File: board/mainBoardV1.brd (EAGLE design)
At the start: 41.9 x 14.9 mm, 11 parts, among them U1 STM32F051C8T

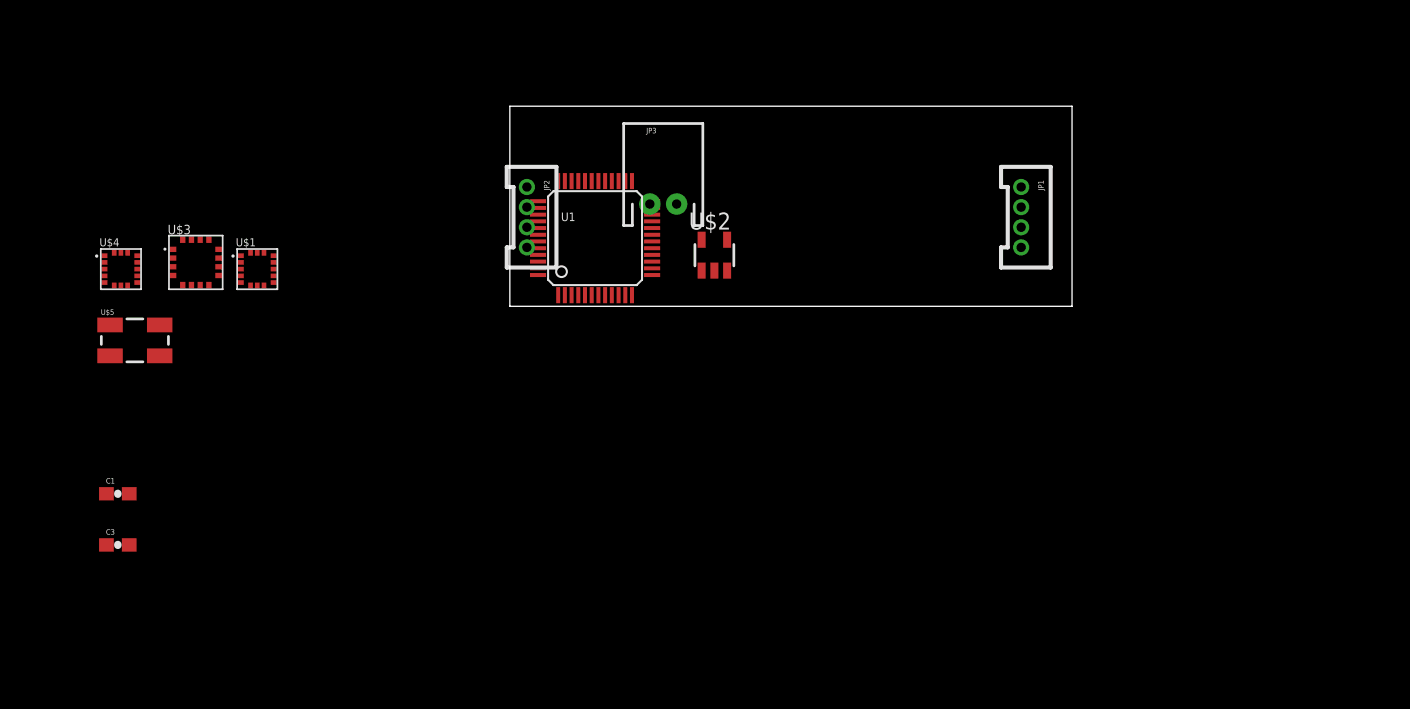
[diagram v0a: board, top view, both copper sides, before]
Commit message: initial board + LPC MCU
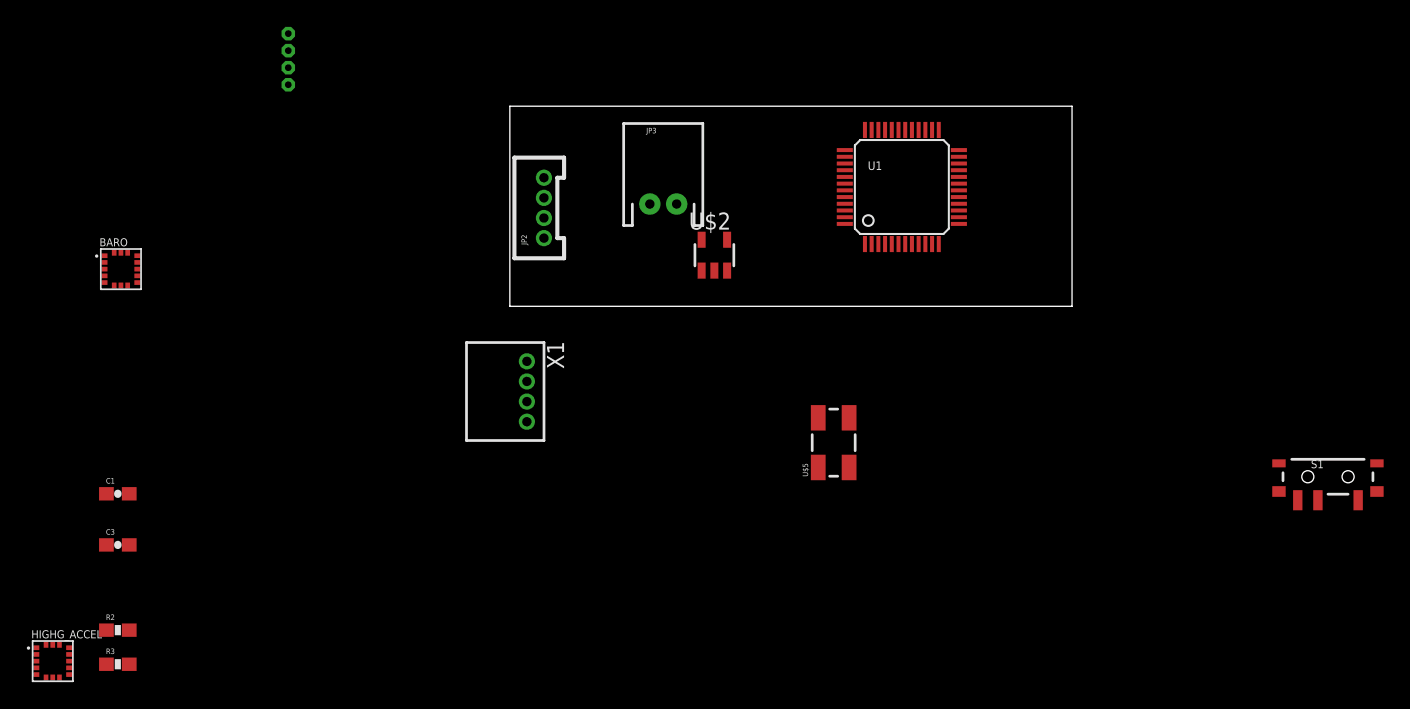
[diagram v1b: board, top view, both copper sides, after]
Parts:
- removed U$1: LIS3DSH, Sensors:LGA-16-3X3X1
- removed U$3: L3G4200D, Sensors:LGA-16L-4X4X1.1
- added HIGHG_ACCEL: LPS331AP, Sensors:LGA-16-3X3X1
- added R2, R3: pullup, SparkFun-Passives:0603-RES
- added S1: (no value), SparkFun-Electromechanical:SWITCH-SPST-SMD-A
- added X1: S4B-ZR, con-jst:S4B-ZR
- JP1: value (none) -> M4; device SparkFun-Connectors:1X04-1.5MM_JST -> Connector:M.5_4
- moved JP1 55.8 mm to (-16.5, 20.3)
- moved U$5 52.6 mm to (24.1, -10.2), turned to 90 degrees
- moved U1 23.2 mm to (29.2, 8.89)
- moved JP2 4.02 mm to (2.54, 5.08), turned to 90 degrees
- renumbered U$4 to BARO
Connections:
- removed net VDD: U1.1, U1.24, U1.48
- removed net VDDA: U1.9
- new net I2C1_SCL: BARO.4, HIGHG_ACCEL.4, R3.2, U1.21
- new net I2C1_SDA: BARO.6, HIGHG_ACCEL.6, R2.2, U1.22
- new net I2C2_SCL: U1.35
- new net I2C2_SDA: U1.36
- new net USART1_RX: U1.31
- new net USART1_TX: U1.30
- net 3.3V: now also BARO.1, BARO.15, HIGHG_ACCEL.1, HIGHG_ACCEL.14, HIGHG_ACCEL.15, R2.1, R3.1, U1.1, U1.24, U1.48, U1.9; no longer U$1.14, U$1.15, U$3.15, U$3.16
- net GND: now also HIGHG_ACCEL.10, HIGHG_ACCEL.12, HIGHG_ACCEL.13, HIGHG_ACCEL.16, HIGHG_ACCEL.5, U1.44, U1.7; no longer U$1.10, U$1.12, U$1.13, U$1.16, U$1.2, U$1.3, U$1.5

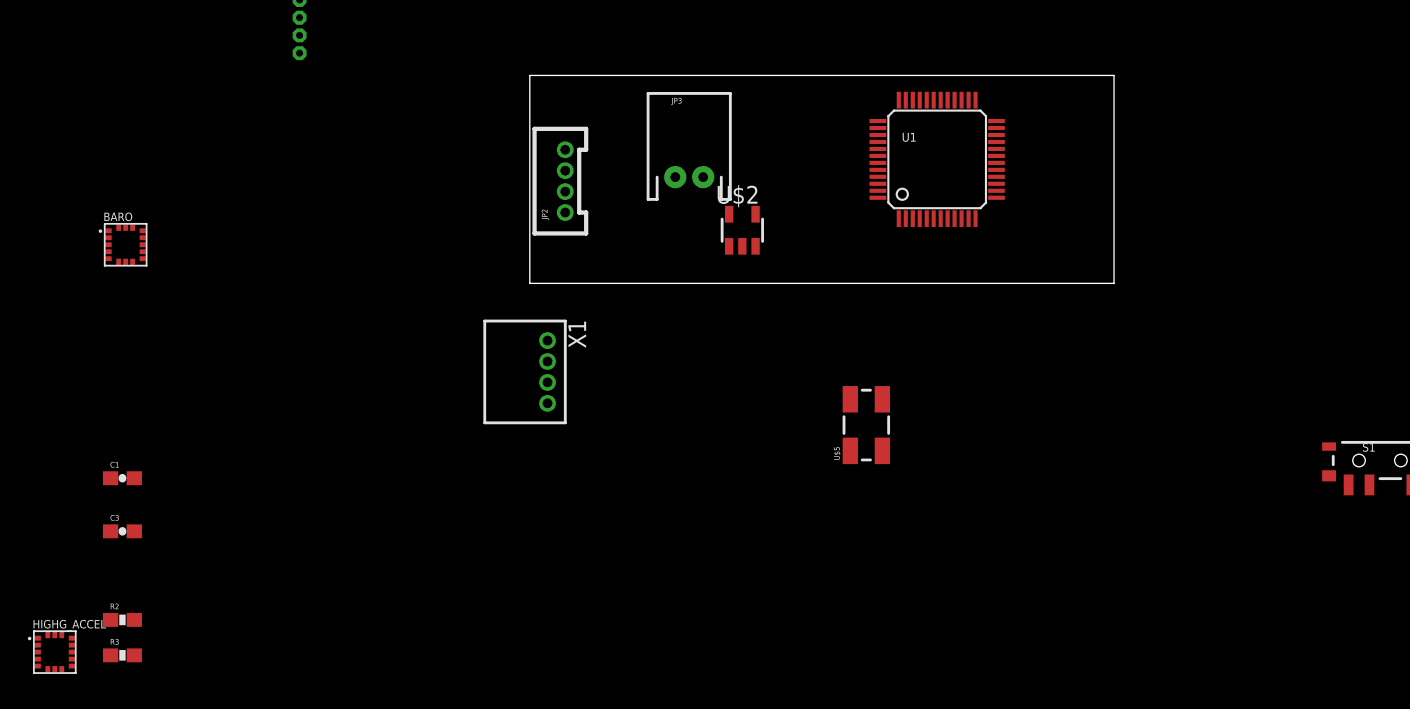
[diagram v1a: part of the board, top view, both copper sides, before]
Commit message: all major components on board, we have very little space
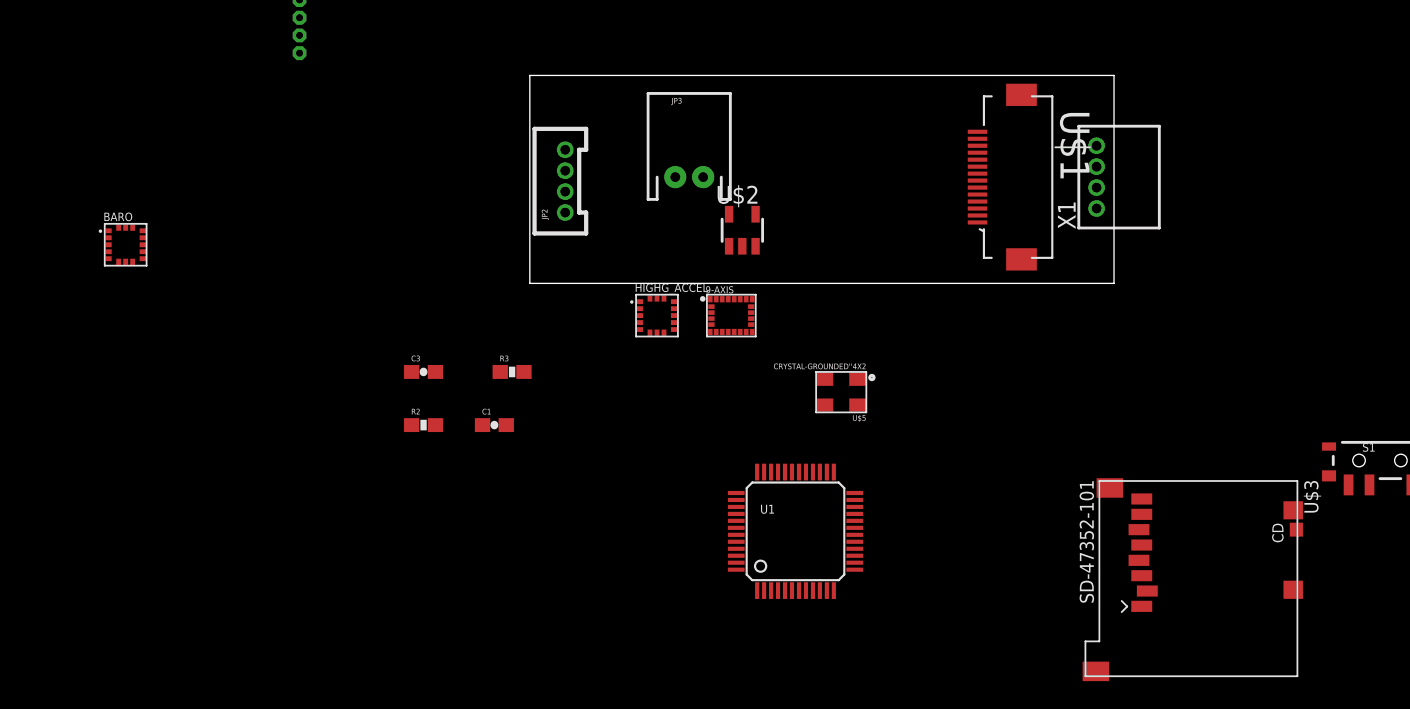
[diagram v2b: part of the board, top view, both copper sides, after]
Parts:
- added 9-AXIS: LSM9DS1, Sensors:LGA-24L-3.5X3X1
- added U$1: ER-OLED0.84-1, Sensors:MOLEX_52892-1433
- added U$3: MICROSD-CD, Sensors:MOLEX_SD-47352-101
- U$5: value CRYSTAL-GROUNDED -> CRYSTAL-GROUNDED''4X2; device SparkFun-FreqCtrl:CRYSTAL-SMD-5X3 -> SparkFun-FreqCtrl:CRYSTAL-SMD-4X2
- U1: value STM32F051C8T -> (none); device STM32F030:LQFP48 -> LPC11U68:LQFP48
- moved HIGHG_ACCEL 49.5 mm to (7.62, -3.81)
- moved X1 41.8 mm to (40.6, 7.62), turned to 90 degrees
- moved R3 34.5 mm to (-1.27, -6.35)
- moved U1 28.5 mm to (19.1, -17.8)
- moved C1 26.9 mm to (-2.54, -10.2)
- moved R2 25.7 mm to (-7.62, -10.2)
- moved C3 24.4 mm to (-7.62, -6.35)
- moved U$5 3.81 mm to (24.1, -6.35), turned to 180 degrees
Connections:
- removed net I2C1_SCL: BARO.4, HIGHG_ACCEL.4, R3.2, U1.21
- removed net I2C1_SDA: BARO.6, HIGHG_ACCEL.6, R2.2, U1.22
- removed net I2C2_SCL: U1.35
- removed net I2C2_SDA: U1.36
- removed net USART1_RX: U1.31
- removed net USART1_TX: U1.30
- new net I2C0_SCL: 9-AXIS.2, BARO.4, HIGHG_ACCEL.4, R3.2, U1.15
- new net I2C0_SDA: 9-AXIS.4, BARO.6, HIGHG_ACCEL.6, R2.2, U1.16
- net 3.3V: no longer U1.1, U1.24, U1.48, U1.9
- net GND: now also U$5.P$1, U$5.P$4; no longer U$5.2, U$5.4, U1.23, U1.44, U1.47, U1.7, U1.8
- net N$2: now also U$5.P$2, U1.7; no longer U$5.3, U1.5
- net N$3: now also U$5.P$3; no longer U$5.1

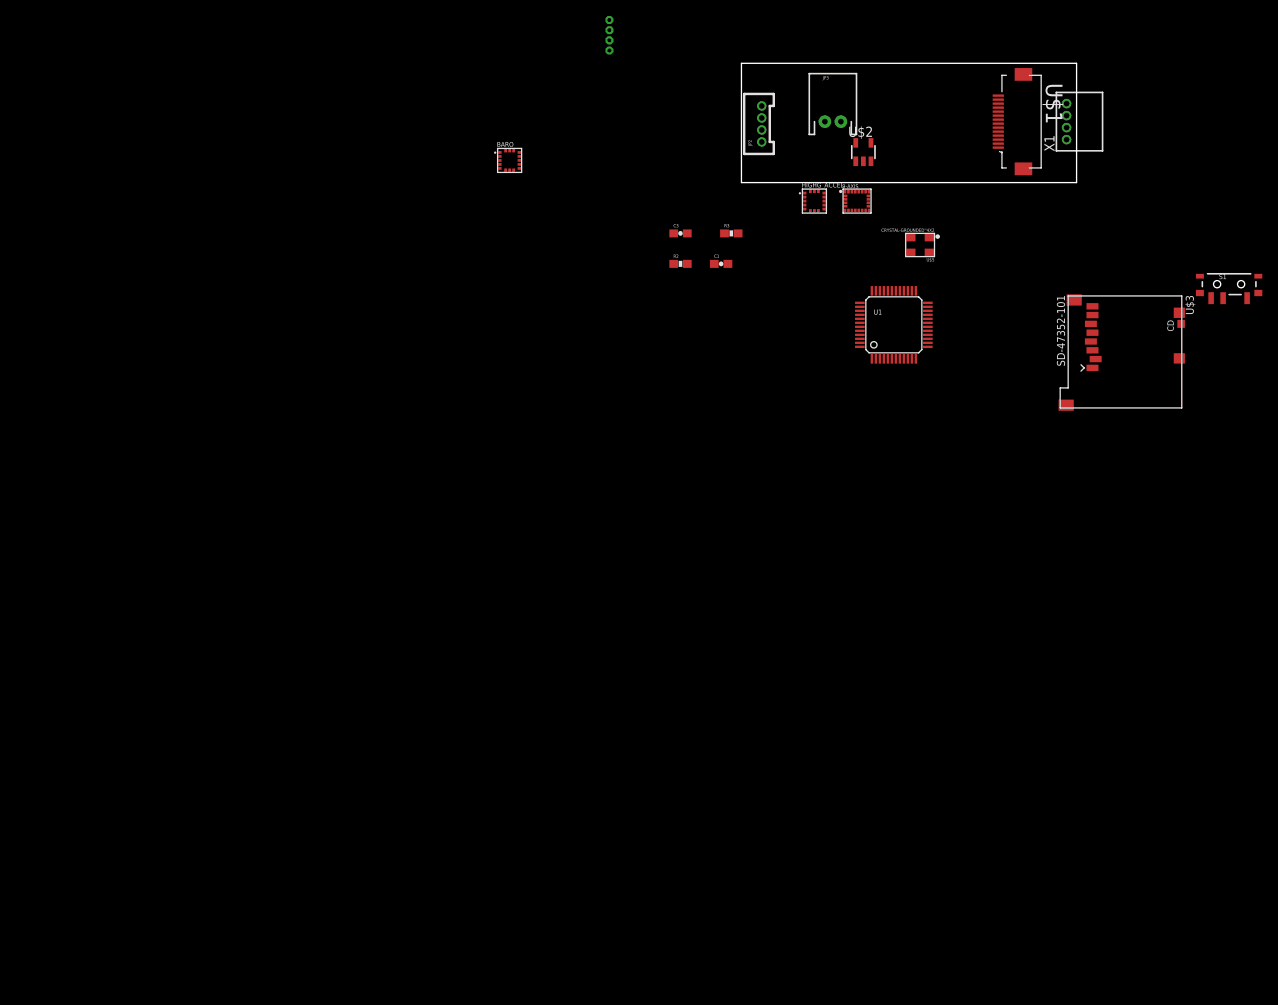
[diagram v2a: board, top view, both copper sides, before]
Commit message: board schematic ready for design review
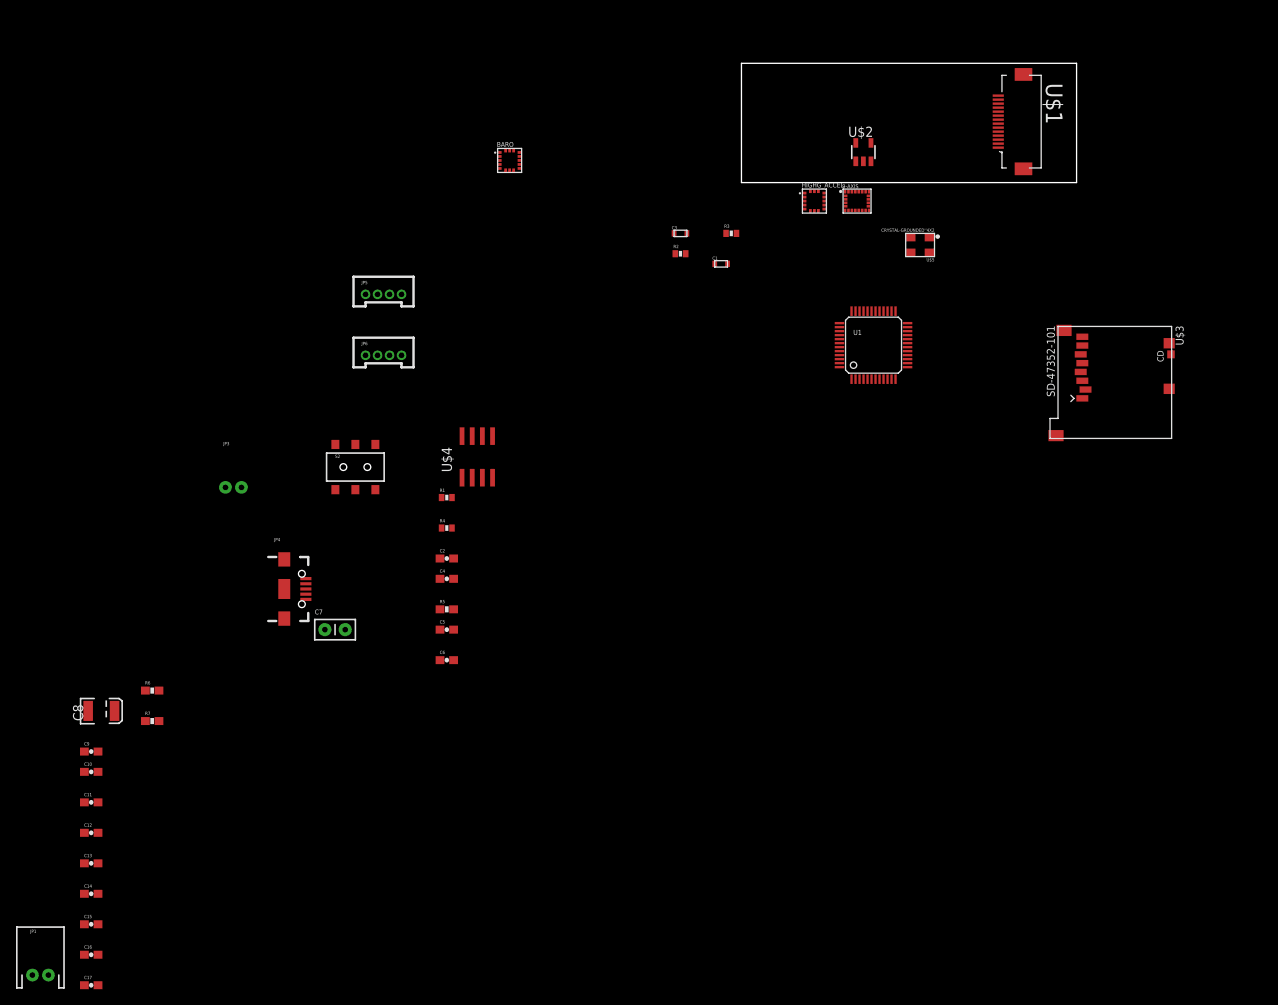
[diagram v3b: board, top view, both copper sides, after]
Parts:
- removed JP2: (no value), SparkFun-Connectors:1X04-1.5MM_JST
- removed S1: (no value), SparkFun-Electromechanical:SWITCH-SPST-SMD-A
- removed X1: S4B-ZR, con-jst:S4B-ZR
- added C10, C14, C15: 1uF, SparkFun-Passives:0603-CAP
- added C11, C16, C17: 0.1uF, SparkFun-Passives:0603-CAP
- added C12, C13, C9: 10uF, SparkFun-Passives:0603-CAP
- added C2, C4: 1uF, SparkFun-Capacitors:0603-CAP
- added C5, C6: 2.2uF, SparkFun-Capacitors:0603-CAP
- added C7: 10nF, SparkFun-Capacitors:CAP-PTH-SMALL2
- added C8: 10uF, SparkFun-Capacitors:EIA3528
- added JP4: USB_MICROB_PLUGCONN-11752, SparkFun-Connectors:USB-B-MICRO-SMD_V03
- added JP5, JP6: (no value), SparkFun-Connectors:1X04-1.5MM_JST
- added R1, R4: pullup, SparkFun-Passives:0402-RES
- added R5: (no value), SparkFun-Resistors:0603-RES
- added R6, R7: 33, SparkFun-Passives:0603-RES
- added S2: DPDT, SparkFun-Electromechanical:AYZ0202
- added U$4: P82B715, Sensors:SO8
- C1, C3: device SparkFun-Passives:0603-CAP -> ELL-i-Passives:C0603
- JP1: value M4 -> M02JST-PTH-2; device Connector:M.5_4 -> SparkFun-Connectors:JST-2-PTH
- JP3: value M02JST-PTH-2 -> M02-JST-2-PTH-NO_SILK; device SparkFun-Connectors:JST-2-PTH -> SparkFun-Connectors:JST-2-PTH-NS
- R2, R3: device SparkFun-Passives:0603-RES -> SparkFun-Passives:0402-RES
- moved JP1 139.0 mm to (-87.6, -99.1), turned to 0 degrees
- moved JP3 87.8 mm to (-63.5, -38.1)
- moved U$3 4.02 mm to (39.4, -17.8)
- moved U1 3.59 mm to (16.5, -20.3)
- moved R2 1.27 mm to (-7.62, -8.89)
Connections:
- new net BARO_INT1: BARO.11, U1.31
- new net BARO_INT2: BARO.9, U1.32
- new net HIGHG_INT1: HIGHG_ACCEL.11, U1.37
- new net HIGHG_INT2: HIGHG_ACCEL.9, U1.38
- new net I2C1_SCL: JP1.1, R4.2, U$1.10, U$4.6, U1.24
- new net I2C1_SDA: JP1.2, R1.2, U$1.11, U$4.3, U1.22
- new net I2CB2B_SCL: JP5.4, JP6.4, U$4.7
- new net I2CB2B_SDA: JP5.3, JP6.3, U$4.2
- new net INT1_A/G: 9-AXIS.11, U1.28
- new net INT2_A/G: 9-AXIS.12, U1.30
- new net INT_M: 9-AXIS.10, U1.33
- new net N$1: JP3.1, S2.1
- new net N$10: C5.1, U$1.13
- new net N$11: 9-AXIS.21, C7.1
- new net N$12: R5.1, U$1.12
- new net N$13: C6.2, U$1.6
- new net N$14: R6.2, U1.20
- new net N$15: JP4.D+1, R6.1
- new net N$16: JP4.D-1, R7.1
- new net N$17: R7.2, U1.19
- new net N$6: C4.1, U$1.1
- new net N$7: C4.2, U$1.2
- new net N$8: C2.1, U$1.3
- new net N$9: C2.2, U$1.4
- new net OLED_RST: U$1.9
- new net SSP1_MISO: U$3.7, U1.29
- new net SSP1_MOSI: U$3.3, U1.17
- new net SSP1_SCK: U$3.5, U1.13
- new net SSP1_SSEL: U$3.2, U1.39
- new net USB_FTOGGLE: S2.5, U1.4
- new net USB_VBUS: JP4.VBUS1, S2.3
- new net VBUS: JP5.1, JP6.1, S2.2, U$2.1, U$2.3
- net 3.3V: now also 9-AXIS.1, 9-AXIS.13, 9-AXIS.22, 9-AXIS.23, 9-AXIS.3, 9-AXIS.5, 9-AXIS.6, 9-AXIS.7, 9-AXIS.8, BARO.7, BARO.8, C10.1, C11.1, C12.1, C13.1, C14.1, C15.1, C16.1, C17.1, C8.A, C9.1, HIGHG_ACCEL.7, HIGHG_ACCEL.8, R1.1, R4.1, S2.6, U$1.14, U$1.5, U$1.8, U$2.5, U$3.4, U$4.8, U1.14, U1.3, U1.34, U1.40, U1.44, U1.47, U1.8
- net GND: now also 9-AXIS.14, 9-AXIS.15, 9-AXIS.16, 9-AXIS.17, 9-AXIS.18, 9-AXIS.19, 9-AXIS.20, C10.2, C11.2, C12.2, C13.2, C14.2, C15.2, C16.2, C17.2, C5.2, C6.1, C7.2, C8.C, C9.2, JP3.2, JP4.GND1, JP4.SHIELD1, JP4.SHIELD2, JP4.SHIELD3, JP5.2, JP6.2, R5.2, S2.4, U$1.7, U$3.6, U$3.G1, U$3.G2, U$3.G3, U$3.G4, U$4.4, U1.2, U1.35, U1.41, U1.43, U1.5

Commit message: added a bunch of library files and docs
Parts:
- added C18: 10uF, ELL-i-Passives:CT3216
- added C19: 10uF, ELL-i-Passives:C0402
- added LED1, LED2: (no value), adafruit:CHIPLED_0603
- added R8, R9: (no value), ELL-i-Passives:R0402
- added S1, S3: SWITCH-MOMENTARY-2-SMD-1101NE, SparkFun-Electromechanical:TACTILE-SWITCH-1101NE
- C1, C3: device ELL-i-Passives:C0603 -> ELL-i-Passives:C0402
- C10, C11, C12, C13, C14, C15, C16, C17, C9: device SparkFun-Passives:0603-CAP -> ELL-i-Passives:C0402
- C2, C4, C5, C6: device SparkFun-Capacitors:0603-CAP -> ELL-i-Passives:C0402
- C7: device SparkFun-Capacitors:CAP-PTH-SMALL2 -> ELL-i-Passives:C0402
- C8: device SparkFun-Capacitors:EIA3528 -> ELL-i-Passives:CT3216
- R1, R2, R3, R4: device SparkFun-Passives:0402-RES -> ELL-i-Passives:R0402
- R5: device SparkFun-Resistors:0603-RES -> ELL-i-Passives:R0402
- R6, R7: device SparkFun-Passives:0603-RES -> ELL-i-Passives:R0402
- moved C17 154.1 mm to (26.5, 9.85), turned to 270 degrees
- moved C16 153.8 mm to (29.7, 9.90), turned to 90 degrees
- moved JP1 147.1 mm to (20.2, 1.00), flipped to the bottom, turned to 180 degrees
- moved C12 142.7 mm to (28.5, 9.90), turned to 90 degrees
- moved C15 136.3 mm to (15.1, 3.60), turned to 270 degrees
- moved C14 132.0 mm to (12.9, 3.60), turned to 270 degrees
- moved C13 130.1 mm to (14.0, 3.60), turned to 270 degrees
- moved C11 127.4 mm to (8.59, 12.8), turned to 270 degrees
- moved R7 126.9 mm to (20.0, 18.2)
- moved C10 125.7 mm to (9.90, 12.8), turned to 270 degrees
- moved C9 124.7 mm to (10.9, 12.8), turned to 270 degrees
- moved R6 117.4 mm to (11.5, 17.3)
- moved C8 110.7 mm to (5.58, 4.23), flipped to the bottom
- moved C7 97.1 mm to (16.1, 13.2), turned to 90 degrees
- moved JP4 93.7 mm to (12.2, 12.2), flipped to the bottom, turned to 270 degrees
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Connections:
- new net LED_PIN: LED2.A, U1.42
- new net N$18: S3.1, U1.27
- new net N$19: S1.1, U1.26
- new net N$4: LED1.C, R8.2
- new net N$5: LED2.C, R9.2
- net 3.3V: now also LED1.A, S1.2, S3.2
- net GND: now also C18.C, C19.2, R8.1, R9.1
- net VBUS: now also C18.A, C19.1
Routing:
- added copper zone on layer 1, net GND
- added copper zone on layer 16, net GND
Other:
- board size 41.9 x 14.9 mm -> 38 x 15 mm

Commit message: up to date board, some changes are still need in schemetic
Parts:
- U$5: value CRYSTAL-GROUNDED''4X2 -> CRYSTAL-GROUNDED2.5X2; device SparkFun-FreqCtrl:CRYSTAL-SMD-4X2 -> SparkFun-FreqCtrl:CRYSTAL-SMD-2.5X2
- moved R2 21.8 mm to (12.6, -0.89)
- moved C18 12.7 mm to (9.88, -3.57)
- moved R5 6.54 mm to (-4.08, 11.7)
- moved C6 5.27 mm to (32.4, -0.44)
- moved U$5 3.94 mm to (28.6, 5.12), turned to 90 degrees
- moved R6 2.30 mm to (9.27, 17.8)
- moved JP4 0.50 mm to (12.2, 12.7)
- moved C1 0.35 mm to (28.7, 4.59)
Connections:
- removed net OLED_RST: U$1.9
- net 3.3V: now also U$1.9; no longer S1.2, S3.2
- net GND: now also S1.2, S3.2, U$5.GND1, U$5.GND2; no longer U$5.P$1, U$5.P$4
- net N$2: now also U$5.P1; no longer U$5.P$2
- net N$3: now also U$5.P2; no longer U$5.P$3
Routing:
- added copper zone on layer 2, net VBUS

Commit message: latest work
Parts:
- moved LED2 21.3 mm to (21.0, 13.9), turned to 90 degrees
- moved BARO 6.43 mm to (11.0, 6.27)
- moved HIGHG_ACCEL 5.41 mm to (14.1, 0.19)
- moved C18 5.20 mm to (10.1, 1.63), turned to 0 degrees
- moved C13 1.90 mm to (12.2, 4.35)
- moved C14 1.90 mm to (11.2, 4.35)
- moved C15 1.90 mm to (13.3, 4.35)
